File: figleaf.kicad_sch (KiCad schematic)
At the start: 5 parts, among them U1 Nice_Nano_V2

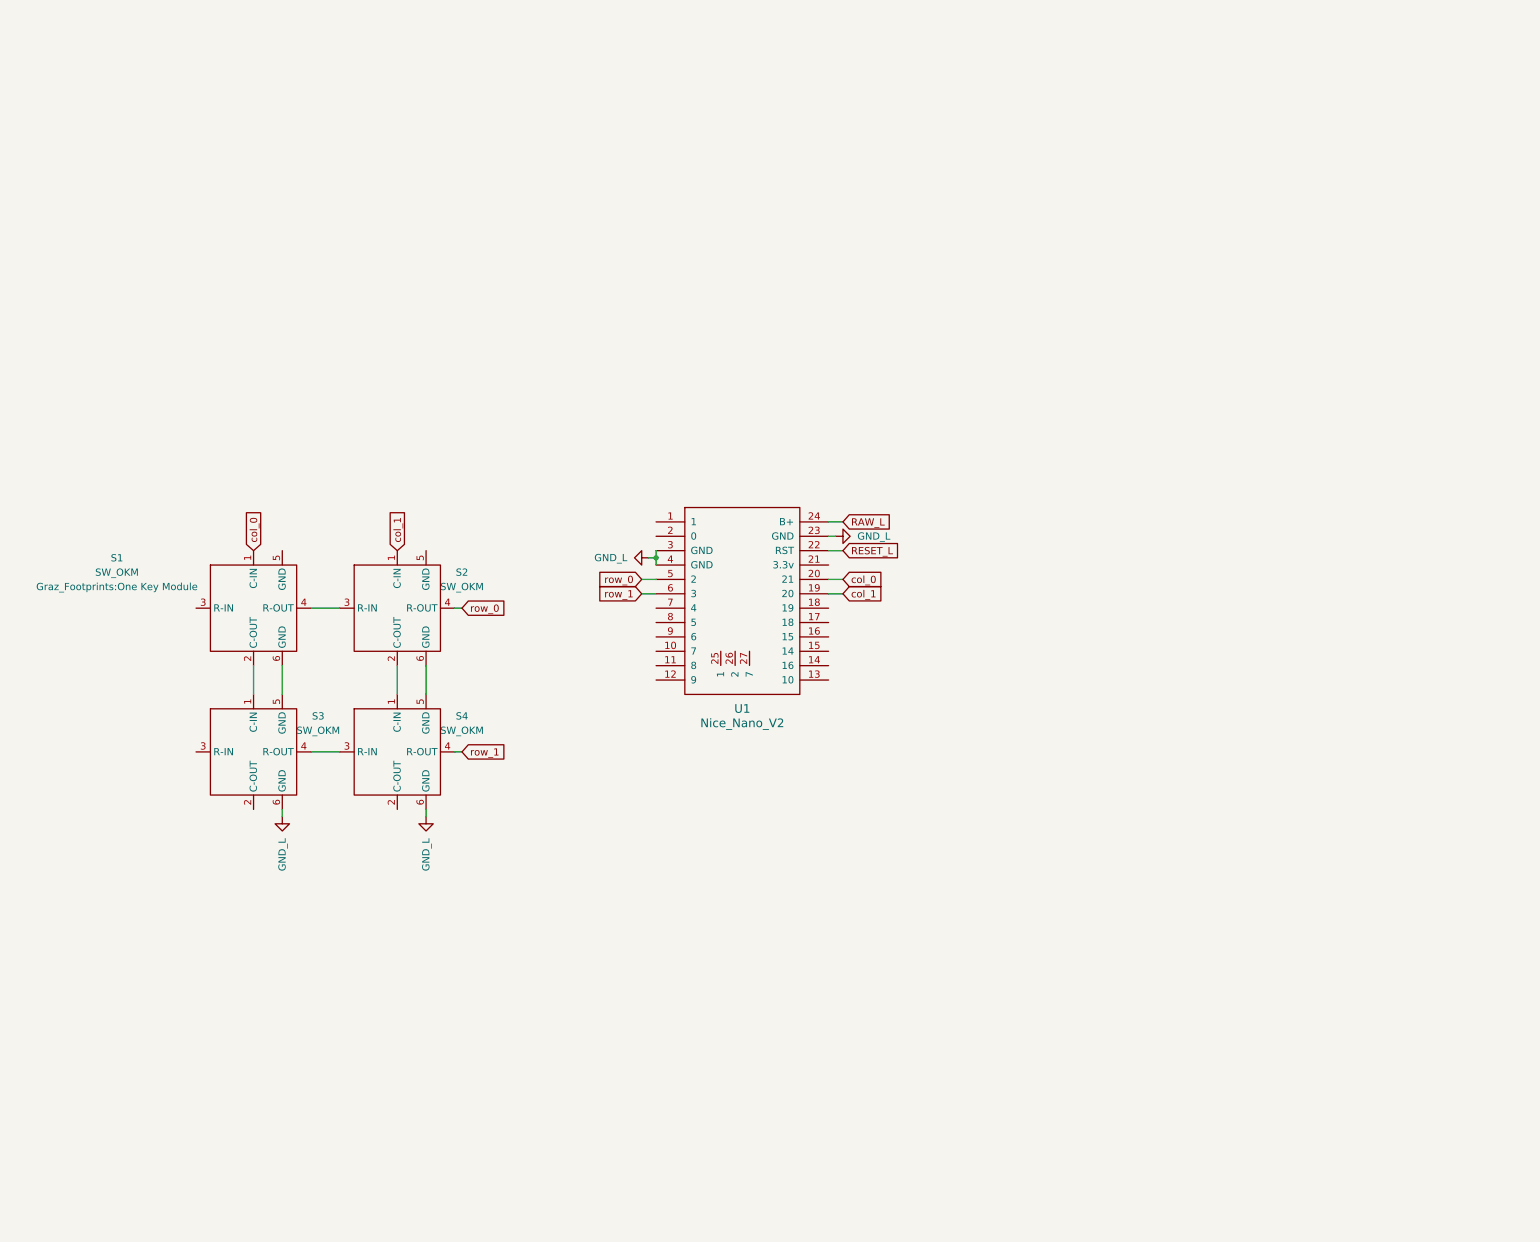
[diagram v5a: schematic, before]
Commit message: add all switches to pcb
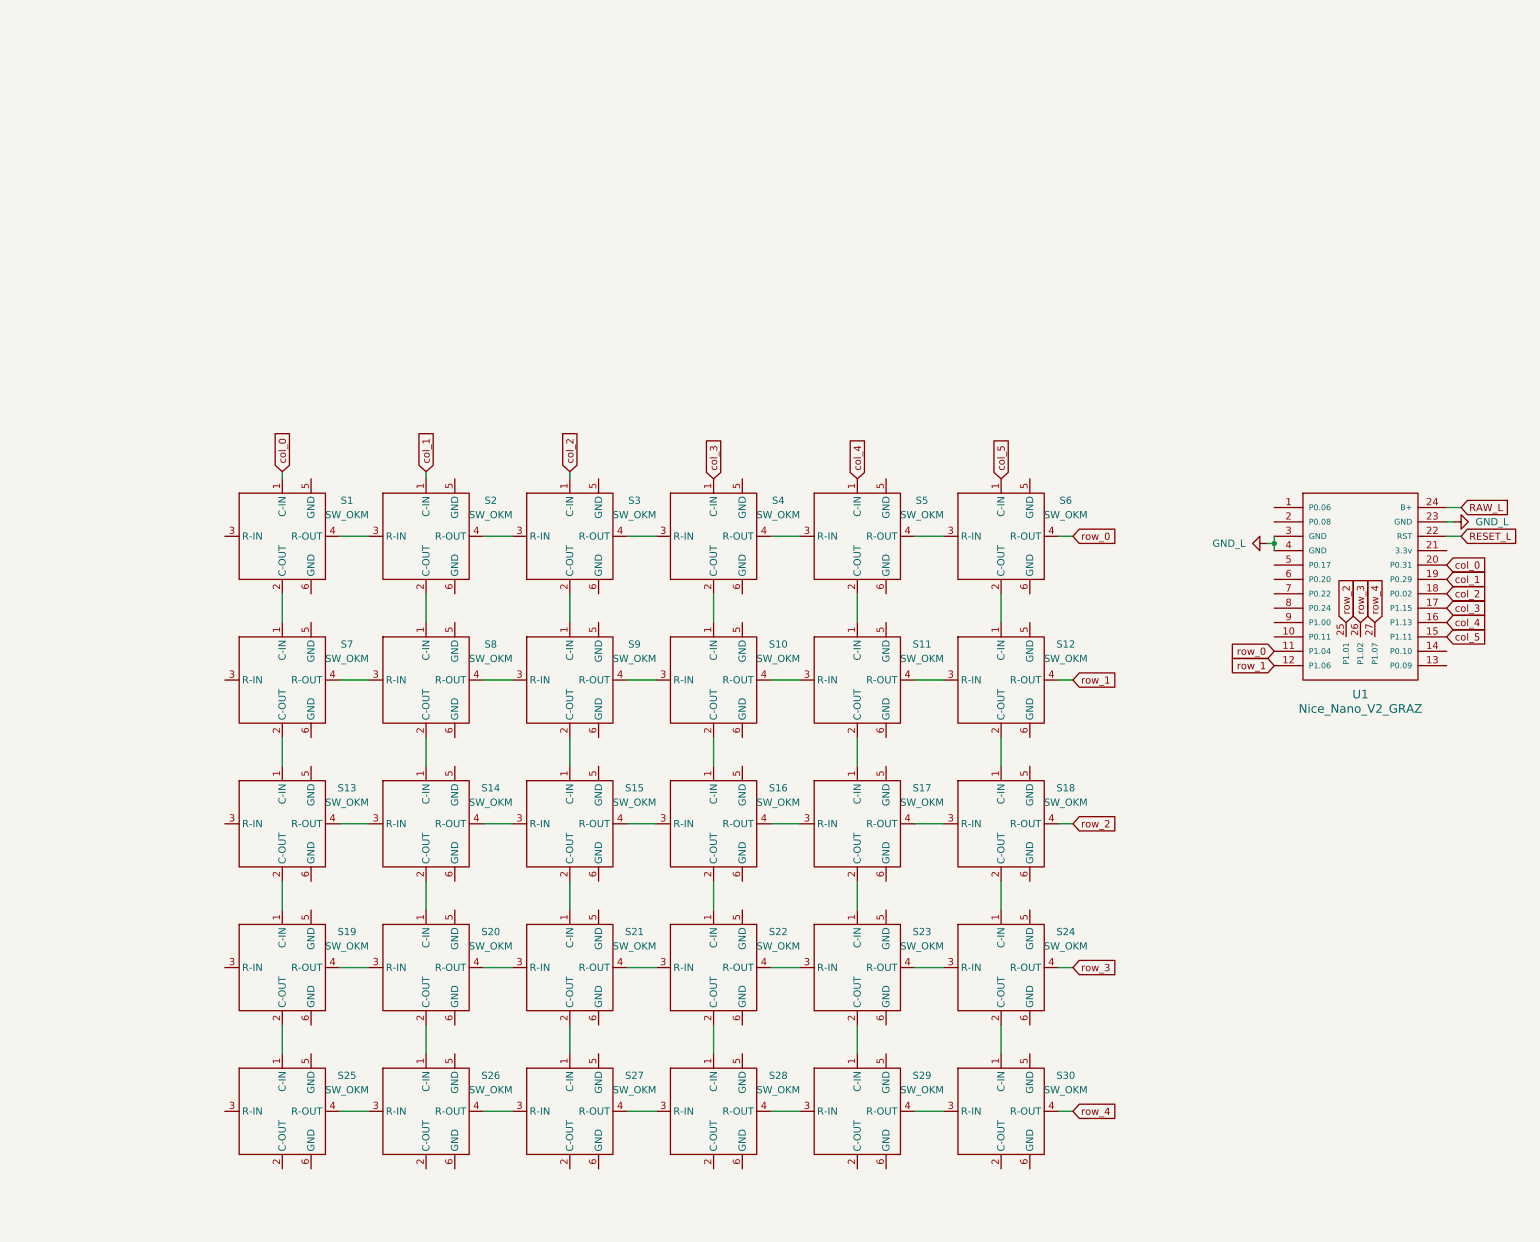
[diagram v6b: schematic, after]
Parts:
- added S10, S11, S12, S13, S14, S15, S16, S17, S18, S19, S20, S21, S22, S23, S24, S25, S26, S27, S28, S29, S30, S5, S6, S7, S8, S9: SW_OKM, Graz_Footprints:One Key Module, symbol 0_graz_symbols:SW_OKM
- U1: value Nice_Nano_V2 -> Nice_Nano_V2_GRAZ; symbol 1_scotto_symbols:MCU_Nice_Nano_V2 -> 0_graz_symbols:MCU_Nice_Nano_V2
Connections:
- net GND_L: no longer S3.6 (GND), S4.6 (GND)
- net row_0: now also U1.11 (P1.04), S6.4 (R-OUT); no longer S2.4 (R-OUT), U1.5 (2)
- net row_1: now also U1.12 (P1.06), S12.4 (R-OUT); no longer S4.4 (R-OUT), U1.6 (3)
- net col_5: now reaches U1.15 (P1.11)
- net col_5: now also S6.1 (C-IN)
- net col_4: now reaches U1.16 (P1.13)
- net col_4: now also S5.1 (C-IN)
- net col_3: now reaches U1.17 (P1.15)
- net col_3: now also S4.1 (C-IN)
- net col_2: now reaches U1.18 (P0.02)
- net col_2: now also S3.1 (C-IN)
- net row_2: now reaches U1.25 (P1.01)
- net row_2: now also S18.4 (R-OUT)
- net row_3: now reaches U1.26 (P1.02)
- net row_3: now also S24.4 (R-OUT)
- net row_4: now reaches U1.27 (P1.07)
- net row_4: now also S30.4 (R-OUT)
- net at S2.2 (C-OUT): now also S8.1 (C-IN); no longer S4.1 (C-IN)
- net at S2.6 (GND): no longer S4.5 (GND)
- net at S1.2 (C-OUT): now also S7.1 (C-IN); no longer S3.1 (C-IN)
- net at S1.6 (GND): no longer S3.5 (GND)
- net at S3.2 (C-OUT): now also S9.1 (C-IN)
- net at S3.3 (R-IN): now also S2.4 (R-OUT)
- net at S4.2 (C-OUT): now also S10.1 (C-IN)
- new net: S13.1 (C-IN), S7.2 (C-OUT)
- new net: S13.2 (C-OUT), S19.1 (C-IN)
- new net: S13.4 (R-OUT), S14.3 (R-IN)
- new net: S14.1 (C-IN), S8.2 (C-OUT)
- new net: S7.4 (R-OUT), S8.3 (R-IN)
- new net: S8.4 (R-OUT), S9.3 (R-IN)
- new net: S10.2 (C-OUT), S16.1 (C-IN)
- new net: S10.3 (R-IN), S9.4 (R-OUT)
- new net: S10.4 (R-OUT), S11.3 (R-IN)
- new net: S16.2 (C-OUT), S22.1 (C-IN)
- new net: S22.2 (C-OUT), S28.1 (C-IN)
- new net: S21.4 (R-OUT), S22.3 (R-IN)
- new net: S22.4 (R-OUT), S23.3 (R-IN)
- new net: S15.1 (C-IN), S9.2 (C-OUT)
- new net: S15.2 (C-OUT), S21.1 (C-IN)
- new net: S21.2 (C-OUT), S27.1 (C-IN)
- new net: S20.4 (R-OUT), S21.3 (R-IN)
- new net: S17.2 (C-OUT), S23.1 (C-IN)
- new net: S23.2 (C-OUT), S29.1 (C-IN)
- new net: S23.4 (R-OUT), S24.3 (R-IN)
- new net: S14.4 (R-OUT), S15.3 (R-IN)
- new net: S15.4 (R-OUT), S16.3 (R-IN)
- new net: S11.1 (C-IN), S5.2 (C-OUT)
- new net: S4.4 (R-OUT), S5.3 (R-IN)
- new net: S5.4 (R-OUT), S6.3 (R-IN)
- new net: S20.2 (C-OUT), S26.1 (C-IN)
- new net: S25.4 (R-OUT), S26.3 (R-IN)
- new net: S26.4 (R-OUT), S27.3 (R-IN)
- new net: S11.2 (C-OUT), S17.1 (C-IN)
- new net: S11.4 (R-OUT), S12.3 (R-IN)
- new net: S28.4 (R-OUT), S29.3 (R-IN)
- new net: S29.4 (R-OUT), S30.3 (R-IN)
- new net: S18.2 (C-OUT), S24.1 (C-IN)
- new net: S24.2 (C-OUT), S30.1 (C-IN)
- new net: S12.1 (C-IN), S6.2 (C-OUT)
- new net: S12.2 (C-OUT), S18.1 (C-IN)
- new net: S14.2 (C-OUT), S20.1 (C-IN)
- new net: S19.2 (C-OUT), S25.1 (C-IN)
- new net: S19.4 (R-OUT), S20.3 (R-IN)
- new net: S16.4 (R-OUT), S17.3 (R-IN)
- new net: S17.4 (R-OUT), S18.3 (R-IN)
- new net: S27.4 (R-OUT), S28.3 (R-IN)
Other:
- moved on the sheet: S1, S2, S3, S4, U1

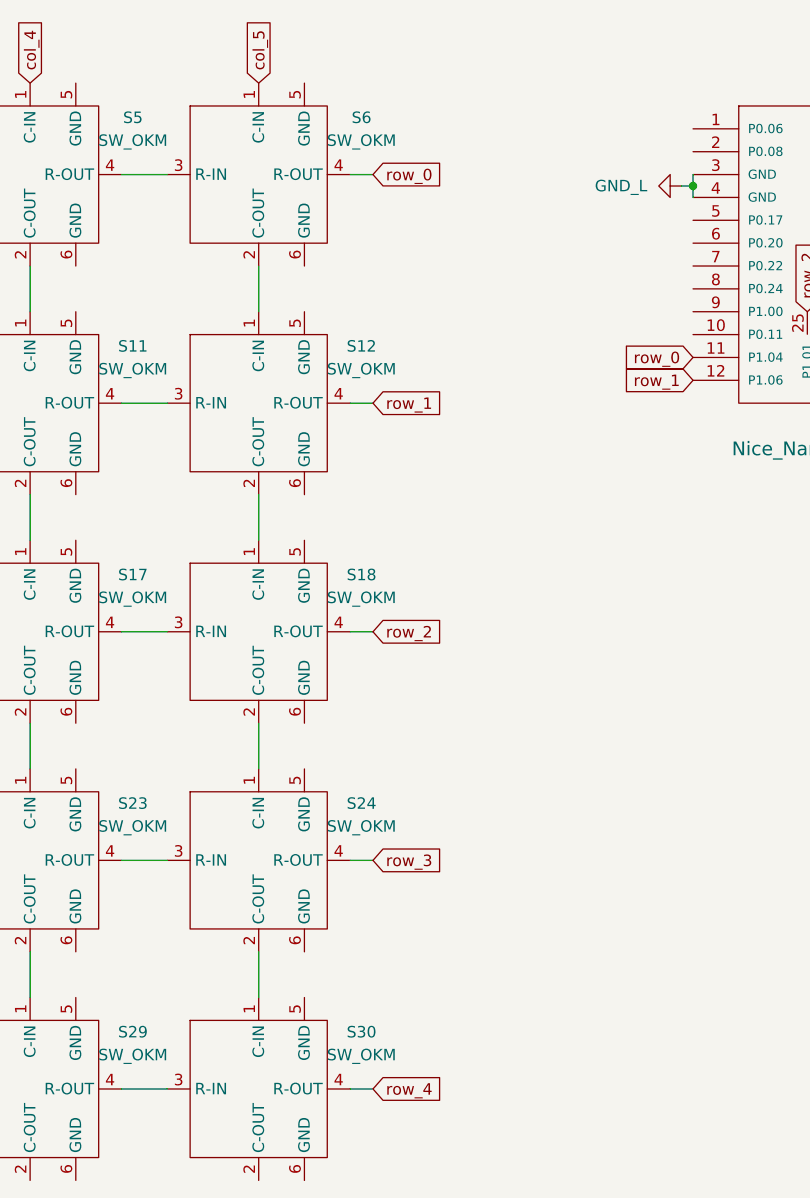
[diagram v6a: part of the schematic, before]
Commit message: PCB progress, switches to 19x19 pitch
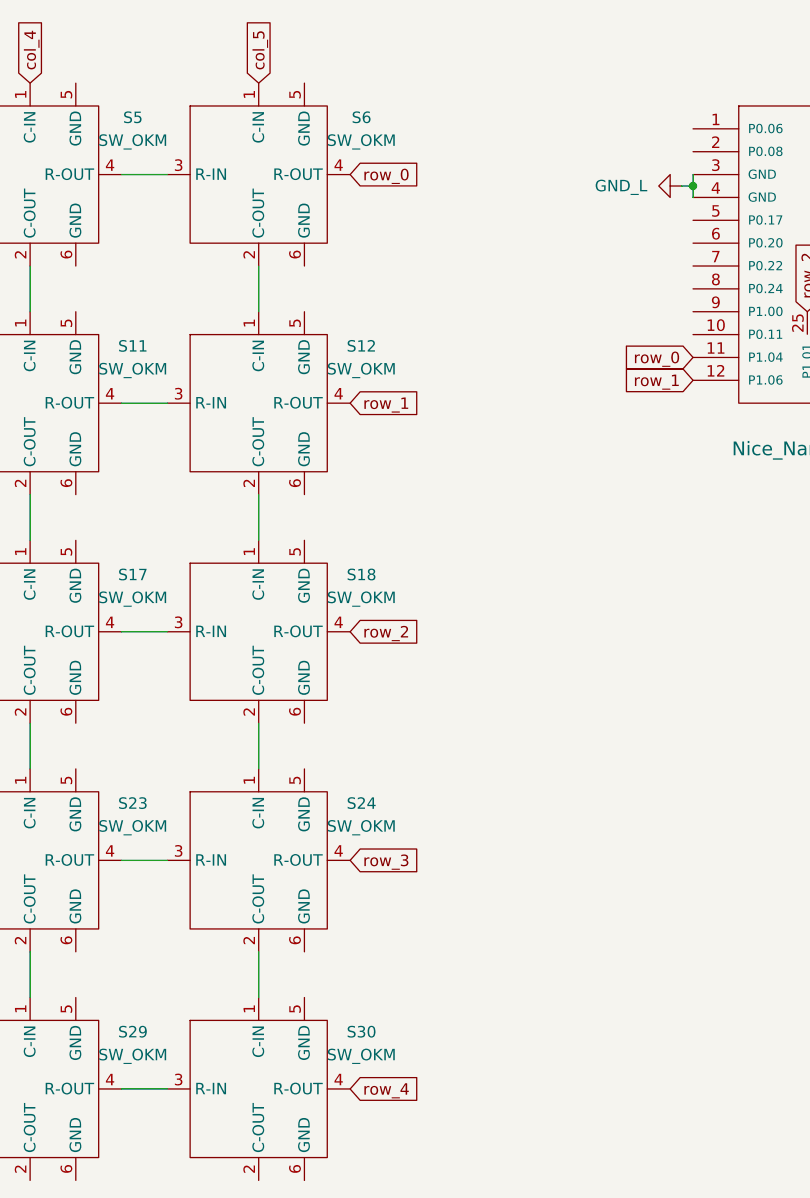
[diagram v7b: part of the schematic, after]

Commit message: Add SW ground conn
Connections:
- net GND_L: now also S1.5 (GND), S2.5 (GND), S25.6 (GND), S26.6 (GND), S27.6 (GND), S28.6 (GND), S29.6 (GND), S3.5 (GND), S30.6 (GND), S4.5 (GND), S5.5 (GND), S6.5 (GND)
- net at S13.5 (GND): now also S7.6 (GND)
- net at S13.6 (GND): now also S19.5 (GND)
- net at S8.5 (GND): now also S2.6 (GND)
- net at S8.6 (GND): now also S14.5 (GND)
- net at S10.5 (GND): now also S4.6 (GND)
- net at S10.6 (GND): now also S16.5 (GND)
- net at S22.5 (GND): now also S16.6 (GND)
- net at S22.6 (GND): now also S28.5 (GND)
- net at S7.5 (GND): now also S1.6 (GND)
- net at S9.5 (GND): now also S3.6 (GND)
- net at S9.6 (GND): now also S15.5 (GND)
- net at S21.5 (GND): now also S15.6 (GND)
- net at S21.6 (GND): now also S27.5 (GND)
- net at S23.5 (GND): now also S17.6 (GND)
- net at S23.6 (GND): now also S29.5 (GND)
- net at S5.6 (GND): now also S11.5 (GND)
- net at S26.5 (GND): now also S20.6 (GND)
- net at S11.6 (GND): now also S17.5 (GND)
- net at S24.5 (GND): now also S18.6 (GND)
- net at S24.6 (GND): now also S30.5 (GND)
- net at S12.5 (GND): now also S6.6 (GND)
- net at S12.6 (GND): now also S18.5 (GND)
- net at S14.6 (GND): now also S20.5 (GND)
- net at S19.6 (GND): now also S25.5 (GND)
- no-connect marks 0 -> 11
